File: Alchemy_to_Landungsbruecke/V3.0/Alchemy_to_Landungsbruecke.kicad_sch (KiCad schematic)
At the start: 2 parts, among them J1 Conn_02x20_Odd_Even, J2 Conn_02x22_Odd_Even

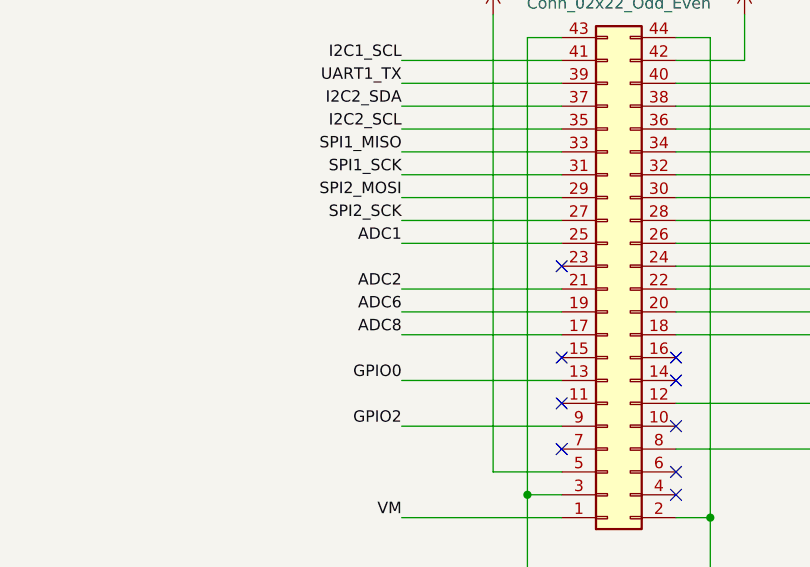
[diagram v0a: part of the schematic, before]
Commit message: Added 0 ohm resistor to GND for LB CLK
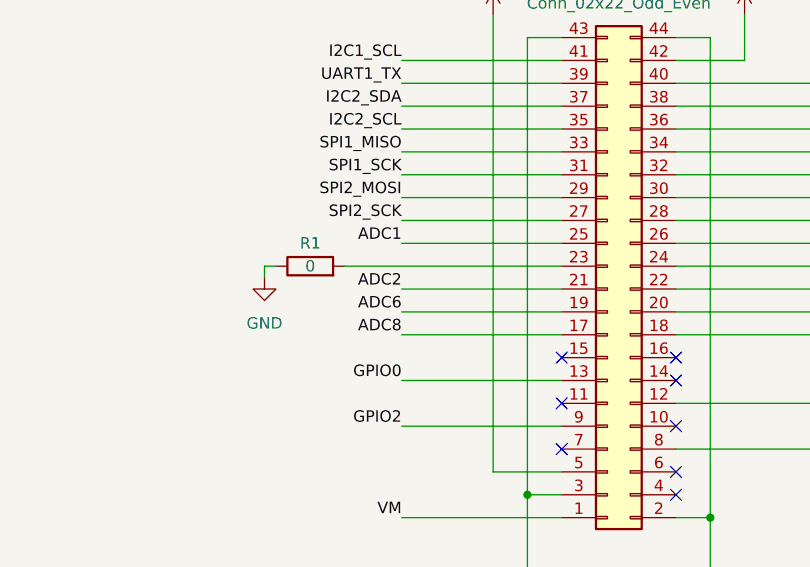
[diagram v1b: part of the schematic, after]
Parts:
- added R1: 0, Resistor_SMD:R_0805_2012Metric, symbol Device:R
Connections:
- net GND: now also R1.1
- net at J2.23 (Pin_23): now also R1.2
- no-connect marks 11 -> 10
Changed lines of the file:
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@@
   (no_connect (at 220.98 127))
   (no_connect (at 220.98 124.46))
-  (no_connect (at 208.28 101.6))
   (wire (pts (xy 190.5 91.44) (xy 208.28 91.44))
     (stroke (width 0) (type default) (color 0 0 0 0))
@@
     (stroke (width 0) (type default) (color 0 0 0 0))
   )
+  (wire (pts (xy 184.15 101.6) (xy 208.28 101.6))
+    (stroke (width 0) (type default) (color 0 0 0 0))
+  )
   (wire (pts (xy 59.69 93.98) (xy 71.12 93.98))
     (stroke (width 0) (type default) (color 0 0 0 0))
@@
     (stroke (width 0) (type default) (color 0 0 0 0))
   )
+  (wire (pts (xy 175.26 101.6) (xy 175.26 102.87))
+    (stroke (width 0) (type default) (color 0 0 0 0))
+  )
   (wire (pts (xy 83.82 93.98) (xy 95.25 93.98))
     (stroke (width 0) (type default) (color 0 0 0 0))
@@
   )
   (wire (pts (xy 220.98 86.36) (xy 238.76 86.36))
+    (stroke (width 0) (type default) (color 0 0 0 0))
+  )
+  (wire (pts (xy 176.53 101.6) (xy 175.26 101.6))
     (stroke (width 0) (type default) (color 0 0 0 0))
   )
@@
     (pin "9")
   )
+  (symbol (lib_id "power:GND") (at 175.26 102.87 0) (unit 1)
+    (in_bom yes) (on_board yes) (fields_autoplaced)
+    (property "Reference" "#PWR0109" (id 0) (at 175.26 109.22 0)
+      (effects (font (size 1.27 1.27)) hide)
+    )
+    (property "Value" "GND" (id 1) (at 175.26 107.95 0))
+    (property "Footprint" "" (id 2) (at 175.26 102.87 0)
+      (effects (font (size 1.27 1.27)) hide)
+    )
+    (property "Datasheet" "" (id 3) (at 175.26 102.87 0)
+      (effects (font (size 1.27 1.27)) hide)
+    )
+    (pin "1")
+  )
   (symbol (lib_id "power:GND") (at 67.31 128.27 0) (unit 1)
     (in_bom yes) (on_board yes) (fields_autoplaced)
@@
     )
     (pin "1")
+  )
+  (symbol (lib_id "Device:R") (at 180.34 101.6 90) (unit 1)
+    (in_bom yes) (on_board yes)
+    (property "Reference" "R1" (id 0) (at 180.34 99.06 90))
+    (property "Value" "0" (id 1) (at 180.34 101.6 90))
+    (property "Footprint" "Resistor_SMD:R_0805_2012Metric" (id 2) (at 180.34 103.378 90)
+      (effects (font (size 1.27 1.27)) hide)
+    )
+    (property "Datasheet" "~" (id 3) (at 180.34 101.6 0)
+      (effects (font (size 1.27 1.27)) hide)
+    )
+    (pin "1")
+    (pin "2")
   )
   (symbol (lib_id "Connector_Generic:Conn_02x22_Odd_Even") (at 213.36 104.14 0) (mirror x) (unit 1)
@@
       (reference "#PWR0108") (unit 1) (value "GND") (footprint "")
     )
+    (path "/4ee25d3b-864d-4632-84dc-69d3de7c9bde"
+      (reference "#PWR0109") (unit 1) (value "GND") (footprint "")
+    )
     (path "/4483d50b-a104-4ad4-b588-ff6ea75a0728"
       (reference "J1") (unit 1) (value "Conn_02x20_Odd_Even") (footprint "pmod-conn_6x2:con_Alchemy_mirrored")
@@
       (reference "J2") (unit 1) (value "Conn_02x22_Odd_Even") (footprint "Connector_PinHeader_2.54mm:PinHeader_2x22_P2.54mm_Vertical")
     )
-  )
+    (path "/c190d89e-9712-4d18-b416-ca3a4a623235"
+      (reference "R1") (unit 1) (value "0") (footprint "Resistor_SMD:R_0805_2012Metric")
+    )
+  )
